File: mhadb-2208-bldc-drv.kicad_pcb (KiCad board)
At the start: 2 copper layers, 47 x 40 mm, 64 parts, among them J1 TC2030, J2 Conn_01x04_Pin, J3 Conn_01x04, M2 Motor_3_Phases, SW1 SW_Push, SW4 SW_Push, U1 AS5600-ASOT, U10 DRV8311H, U2 SN65HVD230, U3 STM32F103C8Tx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

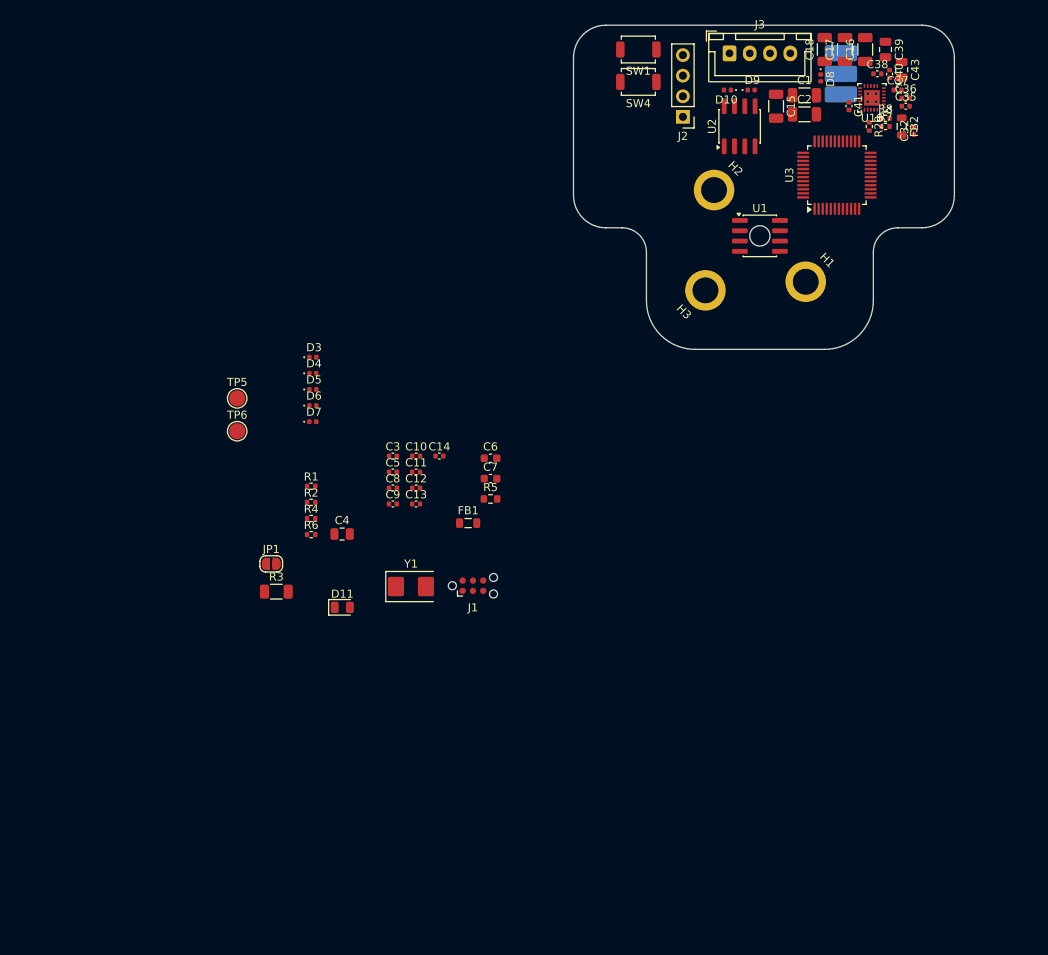
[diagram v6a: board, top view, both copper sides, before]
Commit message: pcb: initial components placement
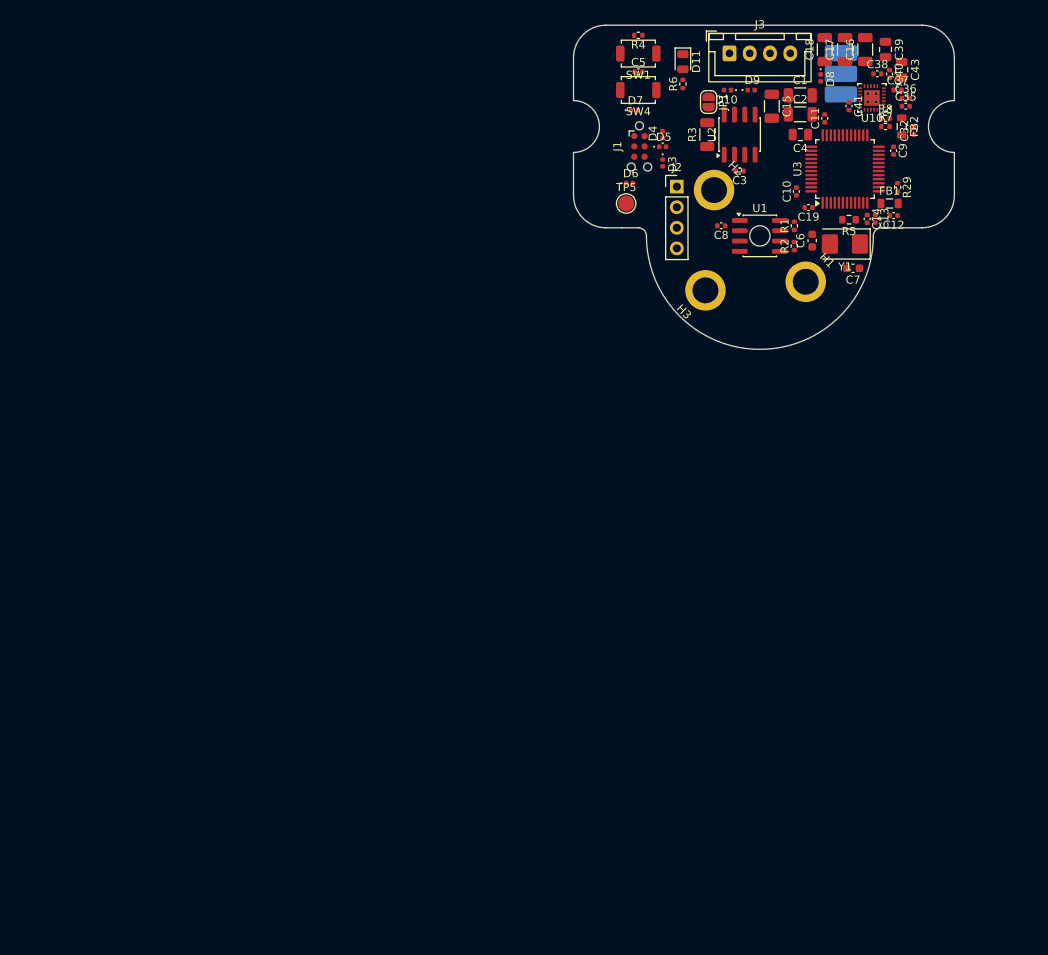
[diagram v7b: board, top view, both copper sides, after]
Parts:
- removed TP6: TestPoint, TestPoint:TestPoint_Pad_D2.0mm
- added C19: 0u1, Capacitor_SMD:C_0402_1005Metric, F.Cu at (125.0, 82.5)
- moved D11 79.4 mm to (109.5, 64.5), turned to -90 degrees
- moved JP1 78.5 mm to (112.7, 69.5), turned to -90 degrees
- moved R3 77.5 mm to (112.5, 73.5), turned to 90 degrees
- moved C9 75.6 mm to (135.5, 75.5), turned to -90 degrees
- moved C4 75.0 mm to (124.0, 73.5), turned to 180 degrees
- moved R6 72.1 mm to (109.5, 67.2), turned to 90 degrees
- moved R4 72.0 mm to (104.0, 61.2), turned to 180 degrees
- moved Y1 68.2 mm to (129.5, 87.0), turned to 180 degrees
- moved C12 67.8 mm to (135.5, 83.5), turned to 180 degrees
- moved R1 67.7 mm to (123.2, 84.8), turned to 90 degrees
- moved R2 67.5 mm to (123.2, 87.2), turned to 90 degrees
- moved C13 66.7 mm to (133.2, 83.9), turned to -90 degrees
- moved C11 66.7 mm to (127.0, 71.5), turned to 90 degrees
- moved FB1 65.3 mm to (135.0, 82.0)
- moved C14 60.4 mm to (132.2, 83.9), turned to -90 degrees
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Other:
- outline, holes or cut-outs redrawn

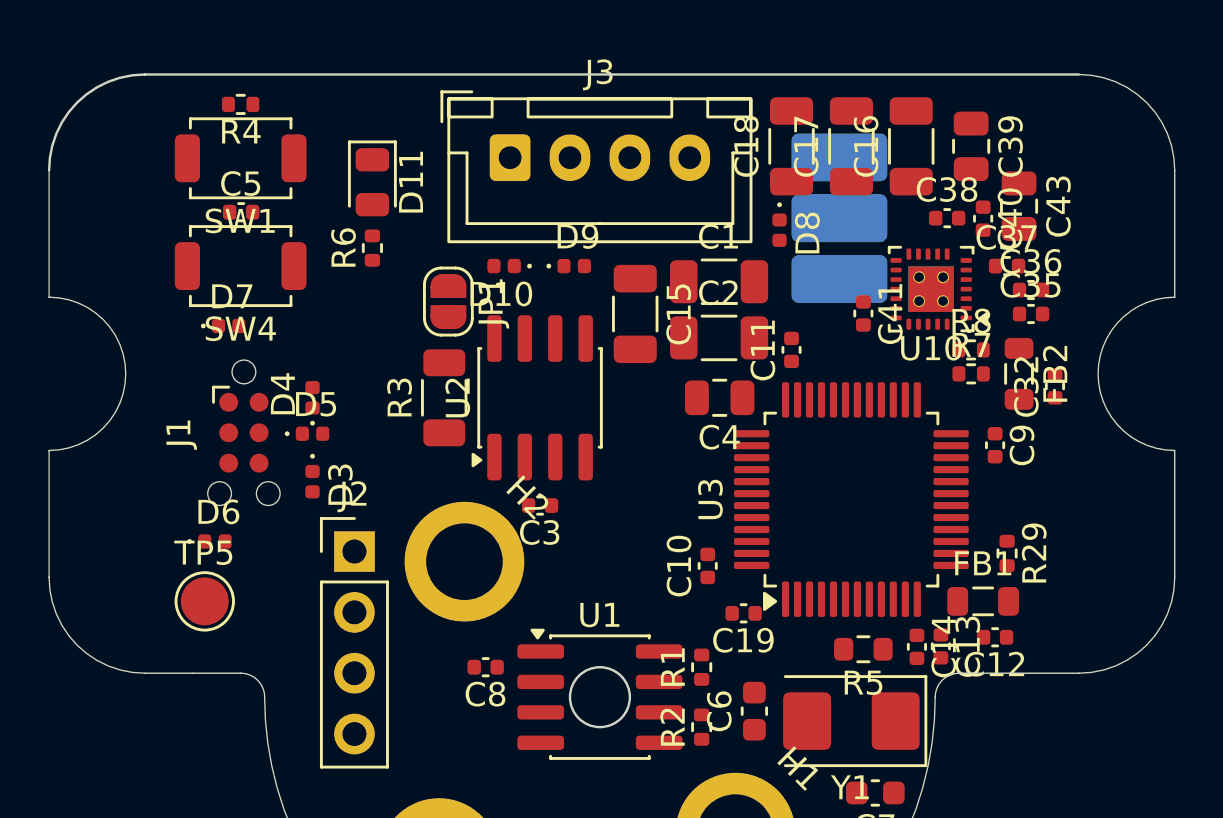
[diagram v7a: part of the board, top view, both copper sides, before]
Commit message: pcb: reduce pcb width to 45m
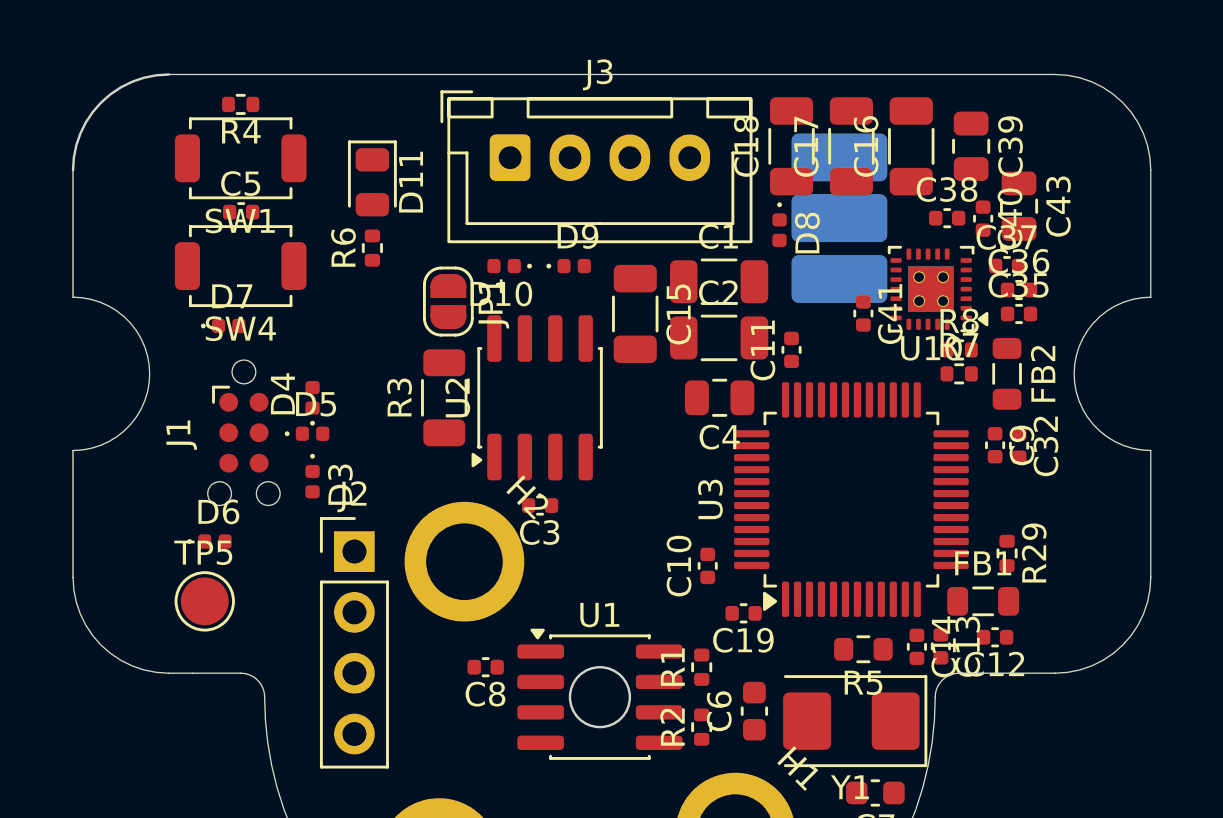
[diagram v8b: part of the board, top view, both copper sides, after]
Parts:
- moved C32 2.90 mm to (136.5, 75.5), turned to -90 degrees
- moved C35 0.50 mm to (136.5, 70.0)
- moved C36 0.50 mm to (136.5, 69.0)
- moved FB2 0.50 mm to (136.0, 72.5)
- moved R7 0.50 mm to (134.0, 72.5)
- moved R8 0.50 mm to (134.0, 71.5)
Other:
- board size 47 x 40 mm -> 45 x 40 mm
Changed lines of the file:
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@@
 	(footprint "Capacitor_SMD:C_0402_1005Metric"
 		(layer "F.Cu")
-		(at 137 69)
+		(at 136.5 69)
 		(descr "Capacitor SMD 0402 (1005 Metric), square (rectangular) end terminal, IPC-7351 nominal, (Body size source: IPC-SM-782 page 76, https://www.pcb-3d.com/wordpress/wp-content/uploads/ipc-sm-782a_amendment_1_and_2.pdf), generated with kicad-footprint-generator")
 		(tags "capacitor")
@@
 	(footprint "Capacitor_SMD:C_0402_1005Metric"
 		(layer "F.Cu")
-		(at 138 73.02 90)
+		(at 136.5 75.5 -90)
 		(descr "Capacitor SMD 0402 (1005 Metric), square (rectangular) end terminal, IPC-7351 nominal, (Body size source: IPC-SM-782 page 76, https://www.pcb-3d.com/wordpress/wp-content/uploads/ipc-sm-782a_amendment_1_and_2.pdf), generated with kicad-footprint-generator")
 		(tags "capacitor")
@@
 		)
 		(property "Basic" "Y"
-			(at 0 0 90)
+			(at 0 0 270)
 			(unlocked yes)
 			(layer "F.Fab")
@@
 		)
 		(property "JLCPCB Part #" "C52923"
-			(at 0 0 90)
+			(at 0 0 270)
 			(unlocked yes)
 			(layer "F.Fab")
@@
 		)
 		(property "Manufacturer" "Samsung Electro-Mechanics "
-			(at 0 0 90)
+			(at 0 0 270)
 			(unlocked yes)
 			(layer "F.Fab")
@@
 		)
 		(property "Manufacturer Part Number" "CL05A105KA5NQNC"
-			(at 0 0 90)
+			(at 0 0 270)
 			(unlocked yes)
 			(layer "F.Fab")
@@
 		(attr smd)
 		(fp_line
-			(start -0.107836 -0.36)
-			(end 0.107836 -0.36)
+			(start -0.107836 0.36)
+			(end 0.107836 0.36)
 			(stroke
 				(width 0.12)
@@
 		)
 		(fp_line
-			(start -0.107836 0.36)
-			(end 0.107836 0.36)
+			(start -0.107836 -0.36)
+			(end 0.107836 -0.36)
 			(stroke
 				(width 0.12)
@@
 		)
 		(pad "1" smd roundrect
-			(at -0.48 0 90)
+			(at -0.48 0 270)
 			(size 0.56 0.62)
 			(layers "F.Cu" "F.Mask" "F.Paste")
@@
 		)
 		(pad "2" smd roundrect
-			(at 0.48 0 90)
+			(at 0.48 0 270)
 			(size 0.56 0.62)
 			(layers "F.Cu" "F.Mask" "F.Paste")
@@
 	(footprint "Inductor_SMD:L_0805_2012Metric"
 		(layer "F.Cu")
-		(at 136.5 72.5 -90)
+		(at 136 72.5 -90)
 		(descr "Inductor SMD 0805 (2012 Metric), square (rectangular) end terminal, IPC-7351 nominal, (Body size source: IPC-SM-782 page 80, https://www.pcb-3d.com/wordpress/wp-content/uploads/ipc-sm-782a_amendment_1_and_2.pdf), generated with kicad-footprint-generator")
 		(tags "inductor")
@@
 	(footprint "Capacitor_SMD:C_0402_1005Metric"
 		(layer "F.Cu")
-		(at 137 70)
+		(at 136.5 70)
 		(descr "Capacitor SMD 0402 (1005 Metric), square (rectangular) end terminal, IPC-7351 nominal, (Body size source: IPC-SM-782 page 76, https://www.pcb-3d.com/wordpress/wp-content/uploads/ipc-sm-782a_amendment_1_and_2.pdf), generated with kicad-footprint-generator")
 		(tags "capacitor")
@@
 	(footprint "Resistor_SMD:R_0402_1005Metric"
 		(layer "F.Cu")
-		(at 134.5 71.5)
+		(at 134 71.5)
 		(descr "Resistor SMD 0402 (1005 Metric), square (rectangular) end terminal, IPC-7351 nominal, (Body size source: IPC-SM-782 page 72, https://www.pcb-3d.com/wordpress/wp-content/uploads/ipc-sm-782a_amendment_1_and_2.pdf), generated with kicad-footprint-generator")
 		(tags "resistor")
@@
 	(footprint "Resistor_SMD:R_0402_1005Metric"
 		(layer "F.Cu")
-		(at 134.5 72.5)
+		(at 134 72.5)
 		(descr "Resistor SMD 0402 (1005 Metric), square (rectangular) end terminal, IPC-7351 nominal, (Body size source: IPC-SM-782 page 72, https://www.pcb-3d.com/wordpress/wp-content/uploads/ipc-sm-782a_amendment_1_and_2.pdf), generated with kicad-footprint-generator")
 		(tags "resistor")
@@
 	)
 	(gr_line
-		(start 96 81)
-		(end 96 75.7)
+		(start 97 81)
+		(end 97 75.7)
 		(stroke
 			(width 0.05)
@@
 	)
 	(gr_line
-		(start 139 85)
+		(start 138 85)
 		(end 134 85)
 		(stroke
@@
 	(gr_line
 		(start 102 85)
-		(end 100 85)
+		(end 101 85)
 		(stroke
 			(width 0.05)
@@
 	)
 	(gr_arc
-		(start 143 81)
-		(mid 141.828427 83.828427)
-		(end 139 85)
+		(start 142 81)
+		(mid 140.828427 83.828427)
+		(end 138 85)
 		(stroke
 			(width 0.05)
@@
 	)
 	(gr_arc
-		(start 96 69.3)
-		(mid 99.2 72.5)
-		(end 96 75.7)
+		(start 97 69.3)
+		(mid 100.2 72.5)
+		(end 97 75.7)
 		(stroke
 			(width 0.05)
@@
 	)
 	(gr_line
-		(start 143 64)
-		(end 143 69.3)
+		(start 142 64)
+		(end 142 69.3)
 		(stroke
 			(width 0.05)
@@
 	)
 	(gr_arc
-		(start 143 75.7)
-		(mid 139.8 72.5)
-		(end 143 69.3)
+		(start 142 75.7)
+		(mid 138.8 72.5)
+		(end 142 69.3)
 		(stroke
 			(width 0.05)
@@
 	)
 	(gr_arc
-		(start 139 60)
-		(mid 141.828427 61.171573)
-		(end 143 64)
+		(start 138 60)
+		(mid 140.828427 61.171573)
+		(end 142 64)
 		(stroke
 			(width 0.05)
@@
 	)
 	(gr_line
-		(start 100 60)
-		(end 139 60)
+		(start 101 60)
+		(end 138 60)
 		(stroke
-			(width 0.1)
-			(type default)
+			(width 0.05)
+			(type solid)
 		)
 		(layer "Edge.Cuts")
 	)
 	(gr_line
-		(start 96 69.3)
-		(end 96 64)
+		(start 97 69.3)
+		(end 97 64)
 		(stroke
 			(width 0.05)
@@
 	)
 	(gr_arc
-		(start 96 64)
-		(mid 97.171573 61.171573)
-		(end 100 60)
+		(start 97 64)
+		(mid 98.171573 61.171573)
+		(end 101 60)
 		(stroke
 			(width 0.1)
@@
 	)
 	(gr_line
-		(start 143 75.7)
-		(end 143 81)
+		(start 142 75.7)
+		(end 142 81)
 		(stroke
 			(width 0.05)
@@
 	)
 	(gr_arc
-		(start 100 85)
-		(mid 97.171573 83.828427)
-		(end 96 81)
+		(start 101 85)
+		(mid 98.171573 83.828427)
+		(end 97 81)
 		(stroke
 			(width 0.05)
@@
 		(polygon
 			(pts
-				(xy 96 60) (xy 100 60) (xy 100 85) (xy 96 85)
+				(xy 97 60) (xy 101 60) (xy 101 85) (xy 97 85)
 			)
 		)
@@
 		(polygon
 			(pts
-				(xy 139 60) (xy 143 60) (xy 143 85) (xy 139 85)
+				(xy 138 60) (xy 142 60) (xy 142 85) (xy 138 85)
 			)
 		)
